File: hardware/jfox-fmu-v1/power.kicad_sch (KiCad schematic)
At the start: 25 parts, among them Q1A PMOS, Q1B PMOS, Q2A PMOS, Q2B PMOS, Q3A PMOS, Q3B PMOS, U20 LTC4417CGN, U21 TPS62132, U22 AP2112K-3.3, U23 AP22804AW5, U24 AP22804AW5, U25 AP22804AW5, U26 AP22804AW5

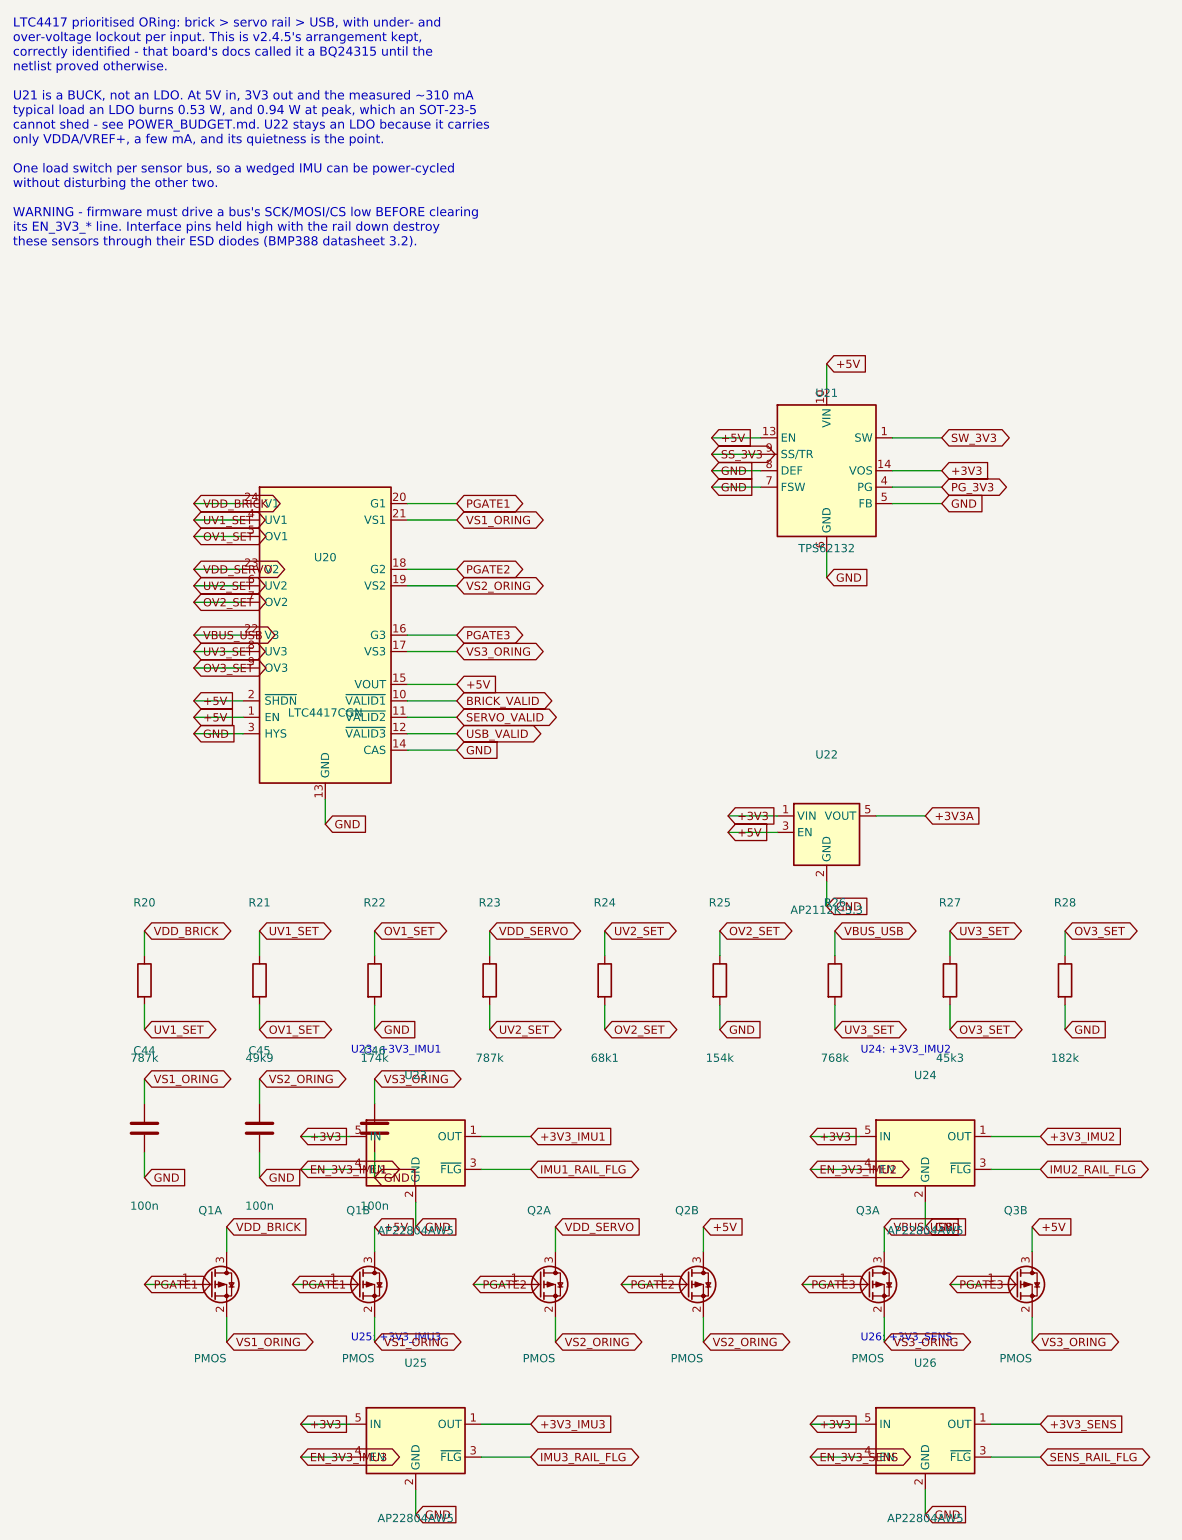
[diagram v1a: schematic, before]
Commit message: Card-cage TMR: FCU becomes a plug-in card, backplane carries the I/O
The FMU stops being a module that mates face-to-face with a base board
underneath it and becomes a card that slides into a backplane. That change
came from the JFOX FCU V1 sketch, and it dissolved a constraint I had
worked around rather than removed: the DF12 mezzanine's 3.0 mm stack height
joins two adjacent boards only, so three channels each needing an
independent path to one base board could not use it. Riser cards were the
workaround. Mating at the card's rear edge means nothing has to span the
gap, so the risers and their extra mated pair per channel are gone.

FCU card, 40 x 90 mm (was 100 x 80):
  * 58-contact Samtec MECF-30 card edge, polarised. Contacts 21/22 are a
    1.24 x 7.0 mm key notch offset from centre - a card the wrong way round
    physically will not enter, which is the only insertion safeguard that
    works before power is applied. Two grounds were sacrificed for it out of
    twenty rather than any signal.
  * Power input tree (LTC4417, six ORing FETs, dividers, input TVS) and the
    debug header move to the backplane. The card receives an already-ORed,
    already-fused +5V_CARRIER on three fingers.
  * Front edge carries everything a person touches: microSD, USB-C, and two
    lamps flanking it. D1 is hardwired to the rail so it lights with no
    firmware running - a power lamp the MCU drives tells you the MCU is
    alive, which is not what anyone reads it for.
  * Power and isolated blocks moved to the back face. Both noise groups are
    grouped at one end so the sensor island can sit 22 mm clear at the
    other; spread out, every point on an 80 mm body is within 13 mm of
    something switching.

JFOX-BASE-v1 backplane, 100 x 100 mm, new:
  * Three independent card-edge sockets in a column. A bent contact in one
    slot costs one channel; a shared bus would cost all three and leave the
    voter nothing to vote on.
  * Two airframe feeds at opposite corners, ORed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
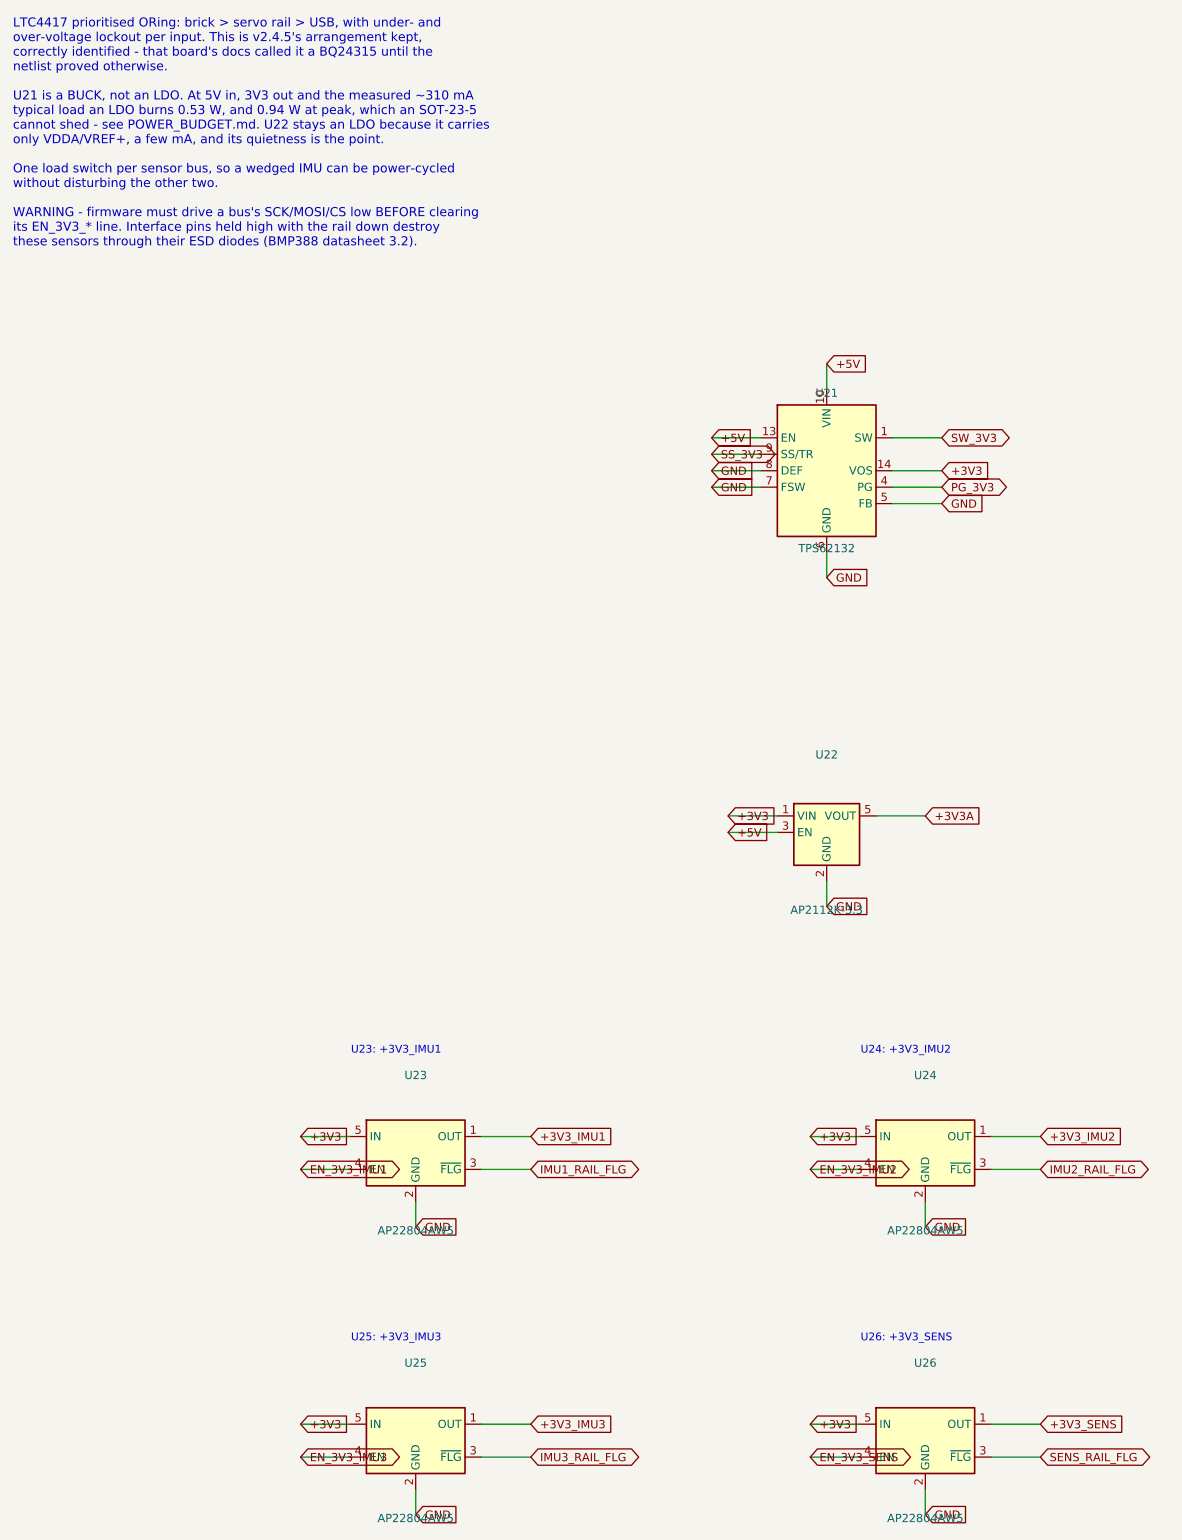
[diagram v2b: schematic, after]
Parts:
- removed C44, C45, C46: 100n, Capacitor_SMD:C_0402_1005Metric, symbol Device:C
- removed Q1A, Q1B, Q2A, Q2B, Q3A, Q3B: PMOS, Package_TO_SOT_SMD:SOT-23, symbol Transistor_FET:Q_PMOS_GSD
- removed R20, R23: 787k, Resistor_SMD:R_0402_1005Metric, symbol Device:R
- removed R21: 49k9, Resistor_SMD:R_0402_1005Metric, symbol Device:R
- removed R22: 174k, Resistor_SMD:R_0402_1005Metric, symbol Device:R
- removed R24: 68k1, Resistor_SMD:R_0402_1005Metric, symbol Device:R
- removed R25: 154k, Resistor_SMD:R_0402_1005Metric, symbol Device:R
- removed R26: 768k, Resistor_SMD:R_0402_1005Metric, symbol Device:R
- removed R27: 45k3, Resistor_SMD:R_0402_1005Metric, symbol Device:R
- removed R28: 182k, Resistor_SMD:R_0402_1005Metric, symbol Device:R
- removed U20: LTC4417CGN, Package_SO:SSOP-24_3.9x8.7mm_P0.635mm, symbol Power_Management:LTC4417CGN
